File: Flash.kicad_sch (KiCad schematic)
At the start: 1 part, among them U3 W25Q32JVSS

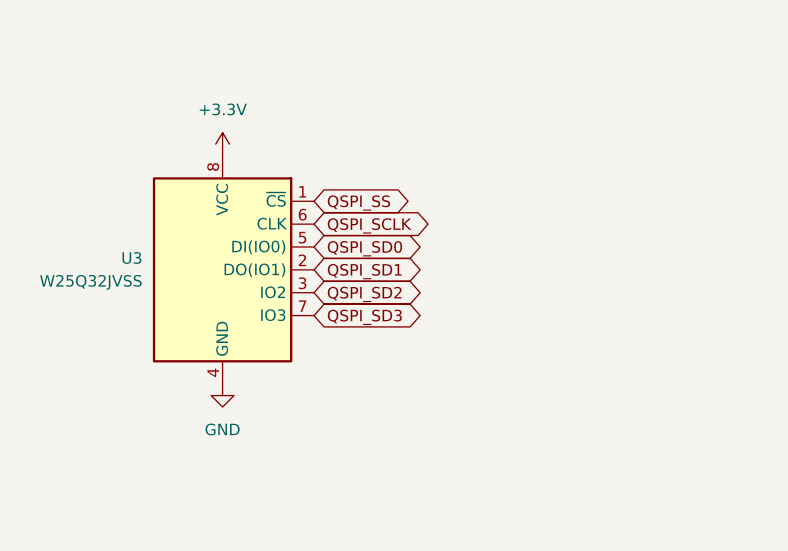
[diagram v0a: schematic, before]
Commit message: flash + bms + usb switch
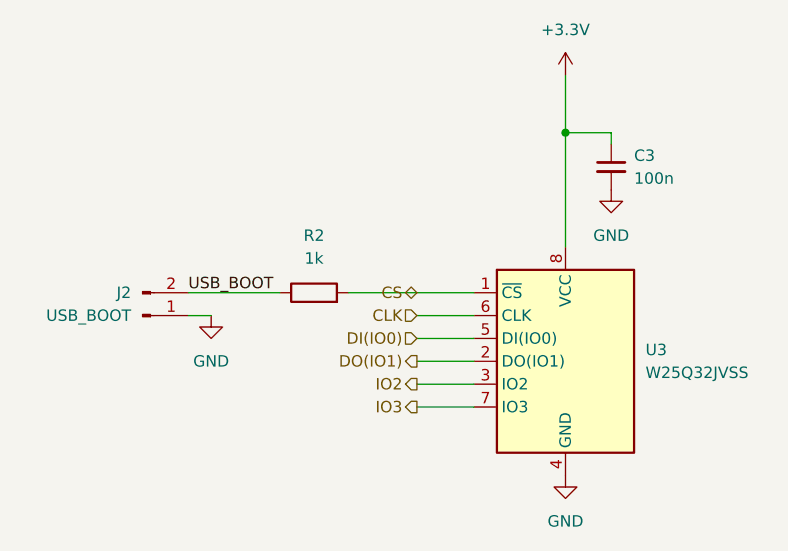
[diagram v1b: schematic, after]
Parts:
- added C3: 100n, symbol Device:C_Small
- added J2: USB_BOOT, symbol Connector:Conn_01x02_Pin
- added R2: 1k, symbol Device:R
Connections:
- net +3.3V: now also C3.1
- net GND: now also C3.2, J2.1 (Pin_1)
- net QSPI_SCLK renamed CLK
- net QSPI_SD0 renamed DI(IO0)
- net QSPI_SD1 renamed DO(IO1)
- net QSPI_SD2 renamed IO2
- net QSPI_SD3 renamed IO3
- net QSPI_SS renamed CS
- net CS: now also R2.2
- new net USB_BOOT: J2.2 (Pin_2), R2.1
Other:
- moved on the sheet: U3

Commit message: cleanup
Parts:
- J2: symbol Connector:Conn_01x02_Pin -> Jumper:Jumper_2_Open
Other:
- moved on the sheet: C3
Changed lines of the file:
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@@
-	(wire
-		(pts
-			(xy 121.92 76.2) (xy 132.08 76.2)
-		)
-		(stroke
-			(width 0)
-			(type default)
-		)
-	)
 	(wire
 		(pts
@@
 	(wire
 		(pts
+			(xy 116.84 88.9) (xy 116.84 86.36)
+		)
+		(stroke
+			(width 0)
+			(type default)
+		)
+	)
+	(wire
+		(pts
 			(xy 153.67 86.36) (xy 147.32 86.36)
 		)
@@
 	(wire
 		(pts
-			(xy 124.46 78.74) (xy 121.92 78.74)
-		)
-		(stroke
-			(width 0)
-			(type default)
-		)
-	)
-	(wire
-		(pts
 			(xy 153.67 88.9) (xy 147.32 88.9)
 		)
@@
 	(wire
 		(pts
-			(xy 168.91 58.42) (xy 168.91 59.69)
+			(xy 171.45 58.42) (xy 171.45 59.69)
 		)
 		(stroke
@@
 	(wire
 		(pts
-			(xy 168.91 58.42) (xy 163.83 58.42)
+			(xy 171.45 58.42) (xy 163.83 58.42)
 		)
 		(stroke
@@
 		)
 	)
+	(wire
+		(pts
+			(xy 116.84 76.2) (xy 132.08 76.2)
+		)
+		(stroke
+			(width 0)
+			(type default)
+		)
+	)
 	(label "USB_BOOT"
-		(at 121.92 76.2 0)
+		(at 119.38 76.2 0)
 		(effects
 			(font
@@
 	(symbol
 		(lib_id "power:GND")
-		(at 124.46 78.74 0)
+		(at 116.84 88.9 0)
 		(unit 1)
 		(exclude_from_sim no)
@@
 		(fields_autoplaced yes)
 		(property "Reference" "#PWR0104"
-			(at 124.46 85.09 0)
+			(at 116.84 95.25 0)
 			(effects
 				(font
@@
 		)
 		(property "Value" "GND"
-			(at 124.46 83.82 0)
-			(effects
-				(font
-					(size 1.27 1.27)
-				)
+			(at 119.38 90.1699 0)
+			(effects
+				(font
+					(size 1.27 1.27)
+				)
+				(justify left)
 			)
 		)
 		(property "Footprint" ""
-			(at 124.46 78.74 0)
+			(at 116.84 88.9 0)
 			(effects
 				(font
@@
 		)
 		(property "Datasheet" ""
-			(at 124.46 78.74 0)
+			(at 116.84 88.9 0)
 			(effects
 				(font
@@
 		)
 		(property "Description" "Power symbol creates a global label with name \"GND\" , ground"
-			(at 124.46 78.74 0)
+			(at 116.84 88.9 0)
 			(effects
 				(font
@@
 	(symbol
 		(lib_id "power:GND")
-		(at 168.91 64.77 0)
+		(at 171.45 64.77 0)
 		(unit 1)
 		(exclude_from_sim no)
@@
 		(fields_autoplaced yes)
 		(property "Reference" "#PWR0107"
-			(at 168.91 71.12 0)
+			(at 171.45 71.12 0)
 			(effects
 				(font
@@
 		)
 		(property "Value" "GND"
-			(at 168.91 69.85 0)
+			(at 171.45 69.85 0)
 			(effects
 				(font
@@
 		)
 		(property "Footprint" ""
-			(at 168.91 64.77 0)
+			(at 171.45 64.77 0)
 			(effects
 				(font
@@
 		)
 		(property "Datasheet" ""
-			(at 168.91 64.77 0)
+			(at 171.45 64.77 0)
 			(effects
 				(font
@@
 		)
 		(property "Description" "Power symbol creates a global label with name \"GND\" , ground"
-			(at 168.91 64.77 0)
+			(at 171.45 64.77 0)
 			(effects
 				(font
@@
 	)
 	(symbol
-		(lib_id "Connector:Conn_01x02_Pin")
-		(at 116.84 78.74 0)
+		(lib_id "Jumper:Jumper_2_Open")
+		(at 116.84 81.28 270)
 		(mirror x)
 		(unit 1)
-		(exclude_from_sim no)
+		(exclude_from_sim yes)
 		(in_bom yes)
 		(on_board yes)
@@
 		(fields_autoplaced yes)
 		(property "Reference" "J2"
-			(at 115.57 76.1999 0)
-			(effects
-				(font
-					(size 1.27 1.27)
-				)
-				(justify right)
+			(at 111.76 81.28 0)
+			(effects
+				(font
+					(size 1.27 1.27)
+				)
 			)
 		)
 		(property "Value" "USB_BOOT"
-			(at 115.57 78.7399 0)
-			(effects
-				(font
-					(size 1.27 1.27)
-				)
-				(justify right)
+			(at 114.3 81.28 0)
+			(effects
+				(font
+					(size 1.27 1.27)
+				)
 			)
 		)
 		(property "Footprint" ""
-			(at 116.84 78.74 0)
+			(at 116.84 81.28 0)
 			(effects
 				(font
@@
 		)
 		(property "Datasheet" "~"
-			(at 116.84 78.74 0)
-			(effects
-				(font
-					(size 1.27 1.27)
-				)
-				(hide yes)
-			)
-		)
-		(property "Description" "Generic connector, single row, 01x02, script generated"
-			(at 116.84 78.74 0)
+			(at 116.84 81.28 0)
+			(effects
+				(font
+					(size 1.27 1.27)
+				)
+				(hide yes)
+			)
+		)
+		(property "Description" "Jumper, 2-pole, open"
+			(at 116.84 81.28 0)
 			(effects
 				(font
@@
 	(symbol
 		(lib_id "Device:C_Small")
-		(at 168.91 62.23 0)
+		(at 171.45 62.23 0)
 		(unit 1)
 		(exclude_from_sim no)
@@
 		(fields_autoplaced yes)
 		(property "Reference" "C3"
-			(at 171.45 60.9662 0)
+			(at 173.99 60.9662 0)
 			(effects
 				(font
@@
 		)
 		(property "Value" "100n"
-			(at 171.45 63.5062 0)
+			(at 173.99 63.5062 0)
 			(effects
 				(font
@@
 		)
 		(property "Footprint" ""
-			(at 168.91 62.23 0)
+			(at 171.45 62.23 0)
 			(effects
 				(font
@@
 		)
 		(property "Datasheet" "~"
-			(at 168.91 62.23 0)
+			(at 171.45 62.23 0)
 			(effects
 				(font
@@
 		)
 		(property "Description" "Unpolarized capacitor, small symbol"
-			(at 168.91 62.23 0)
-			(effects
-				(font
+			(at 171.45 62.23 0)
+			(effects
+				(font

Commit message: BMS updates
Added missing capacitor for OTG
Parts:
- C7: renamed from C3; value 100n -> 0.1μF
- R4: renamed from R2; value 1k -> 1kΩ
- renumbered U3 to U2
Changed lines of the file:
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@@
 		(dnp no)
 		(fields_autoplaced yes)
-		(property "Reference" "#PWR0106"
+		(property "Reference" "#PWR022"
 			(at 163.83 102.87 0)
 			(effects
@@
 			(project "Minibadge Display 5x3"
 				(path "/e5119d15-74fb-4259-abbc-5cab1f368532/72dbc5c2-e6c3-4b41-8ecd-db82b0a9ba3e"
-					(reference "#PWR0106")
+					(reference "#PWR022")
 					(unit 1)
 				)
@@
 		(dnp no)
 		(fields_autoplaced yes)
-		(property "Reference" "#PWR0104"
+		(property "Reference" "#PWR020"
 			(at 116.84 95.25 0)
 			(effects
@@
 			(project ""
 				(path "/e5119d15-74fb-4259-abbc-5cab1f368532/72dbc5c2-e6c3-4b41-8ecd-db82b0a9ba3e"
-					(reference "#PWR0104")
+					(reference "#PWR020")
 					(unit 1)
 				)
@@
 		(dnp no)
 		(fields_autoplaced yes)
-		(property "Reference" "#PWR0105"
+		(property "Reference" "#PWR021"
 			(at 163.83 55.88 0)
 			(effects
@@
 			(project "Minibadge Display 5x3"
 				(path "/e5119d15-74fb-4259-abbc-5cab1f368532/72dbc5c2-e6c3-4b41-8ecd-db82b0a9ba3e"
-					(reference "#PWR0105")
+					(reference "#PWR021")
 					(unit 1)
 				)
@@
 		(dnp no)
 		(fields_autoplaced yes)
-		(property "Reference" "#PWR0107"
+		(property "Reference" "#PWR023"
 			(at 171.45 71.12 0)
 			(effects
@@
 			(project ""
 				(path "/e5119d15-74fb-4259-abbc-5cab1f368532/72dbc5c2-e6c3-4b41-8ecd-db82b0a9ba3e"
-					(reference "#PWR0107")
+					(reference "#PWR023")
 					(unit 1)
 				)
@@
 		(dnp no)
 		(fields_autoplaced yes)
-		(property "Reference" "R2"
+		(property "Reference" "R4"
 			(at 135.89 69.85 90)
 			(effects
@@
 			)
 		)
-		(property "Value" "1k"
+		(property "Value" "1kΩ"
 			(at 135.89 72.39 90)
 			(effects
@@
 			(project ""
 				(path "/e5119d15-74fb-4259-abbc-5cab1f368532/72dbc5c2-e6c3-4b41-8ecd-db82b0a9ba3e"
-					(reference "R2")
+					(reference "R4")
 					(unit 1)
 				)
@@
 		(dnp no)
 		(fields_autoplaced yes)
-		(property "Reference" "C3"
+		(property "Reference" "C7"
 			(at 173.99 60.9662 0)
 			(effects
@@
 			)
 		)
-		(property "Value" "100n"
+		(property "Value" "0.1μF"
 			(at 173.99 63.5062 0)
 			(effects
@@
 			(project ""
 				(path "/e5119d15-74fb-4259-abbc-5cab1f368532/72dbc5c2-e6c3-4b41-8ecd-db82b0a9ba3e"
-					(reference "C3")
+					(reference "C7")
 					(unit 1)
 				)
@@
 		(on_board yes)
 		(dnp no)
-		(property "Reference" "U3"
+		(property "Reference" "U2"
 			(at 172.72 82.5499 0)
 			(effects
@@
 			(project "Minibadge Display 5x3"
 				(path "/e5119d15-74fb-4259-abbc-5cab1f368532/72dbc5c2-e6c3-4b41-8ecd-db82b0a9ba3e"
-					(reference "U3")
-					(unit 1)
-				)
+					(reference "U2")
+					(unit 1)
+				)
